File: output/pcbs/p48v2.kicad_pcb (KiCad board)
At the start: 2 copper layers, 255 x 72 mm, 147 parts, among them U1 Pico2, U2 SSD1306_OLED_1.3

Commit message: Remove Adafruit SSD1306 module (U2) from PCB
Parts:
- removed U2: SSD1306_OLED_1.3, Display:Adafruit_SSD1306_No_Mounting_Holes
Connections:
- U1 pad 26: I2C_SDA -> (no net)
- U1 pad 27: I2C_SCL -> (no net)
- U1 pad 40: VBUS -> (no net)
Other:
- net class Default removed
- net class Power removed

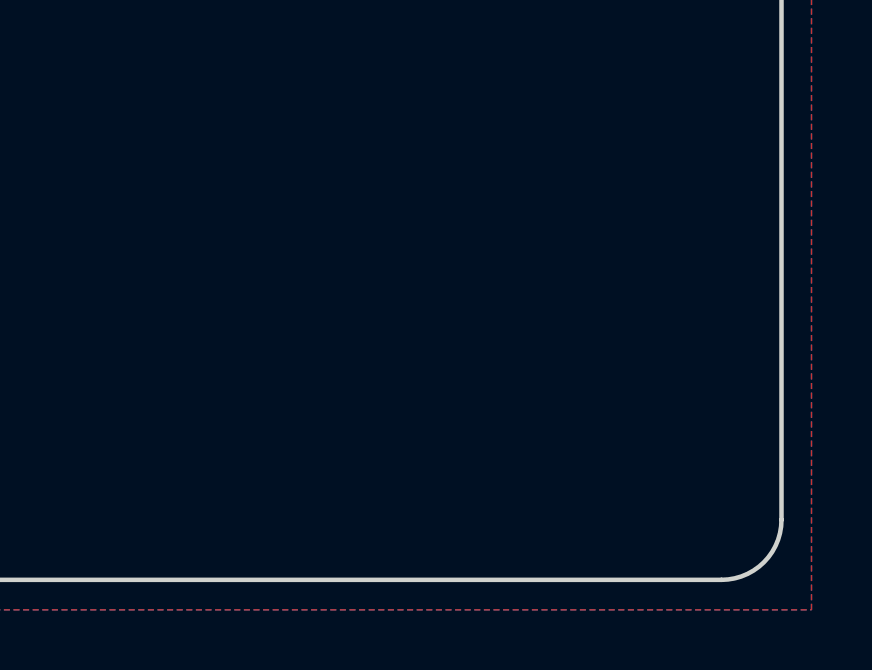
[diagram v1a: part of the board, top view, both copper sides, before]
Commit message: Place FPC connector J1 and OLED passives (C1-C6, R1-R3) on F.Cu
J1: Hirose FH12-30S-0.5SH 30-pin FPC ZIF at (333, -19)
- All 30 pins + 2 MP pads with net assignments for I2C mode
- BS0/BS1/BS2=GND (I2C), D/C=GND (addr 0x3C)
- D0=I2C_SCL, D1+D2=I2C_SDA

Passives clustered around J1:
- C1,C2: 1uF charge pump caps (C1P/C1N, C2P/C2N)
- C3: 4.7uF VCOMH bypass, C4: 2.2uF VBAT bypass
- C5,C6: 100nF VDD/VCC decoupling
- R1: 910k IREF, R2,R3: 4.7k I2C pull-ups

Placed via direct S-expression editing (MCP place_component
couldn't find footprints from standard KiCad libraries).
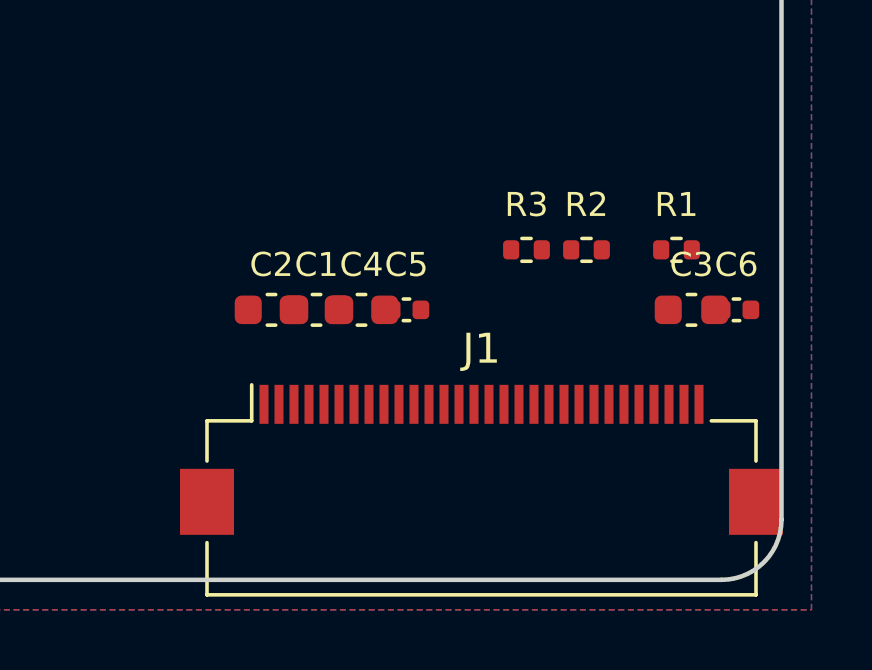
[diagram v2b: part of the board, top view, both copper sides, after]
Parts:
- added C1: 1uF, Capacitor_SMD:C_0603_1608Metric, F.Cu at (327.5, -24.0)
- added C2: 1uF, Capacitor_SMD:C_0603_1608Metric, F.Cu at (326.0, -24.0)
- added C3: 4.7uF, Capacitor_SMD:C_0603_1608Metric, F.Cu at (340.0, -24.0)
- added C4: 2.2uF, Capacitor_SMD:C_0603_1608Metric, F.Cu at (329.0, -24.0)
- added C5: 100nF, Capacitor_SMD:C_0402_1005Metric, F.Cu at (330.5, -24.0)
- added C6: 100nF, Capacitor_SMD:C_0402_1005Metric, F.Cu at (341.5, -24.0)
- added J1: FPC_30pin_0.5mm, Connector_FFC-FPC:Hirose_FH12-30S-0.5SH_1x30-1MP_P0.50mm_Horizontal, F.Cu at (333.0, -19.0)
- added R1: 910k, Resistor_SMD:R_0402_1005Metric, F.Cu at (339.5, -26.0)
- added R2: 4.7k, Resistor_SMD:R_0402_1005Metric, F.Cu at (336.5, -26.0)
- added R3: 4.7k, Resistor_SMD:R_0402_1005Metric, F.Cu at (334.5, -26.0)

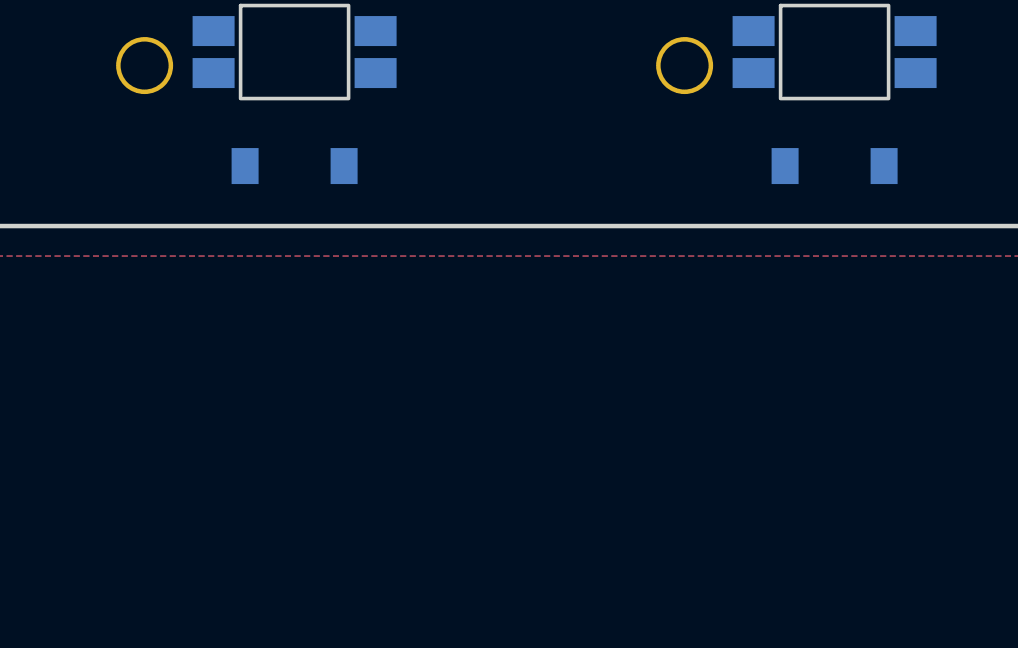
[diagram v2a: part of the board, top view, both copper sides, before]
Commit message: Add USB-C power input for LED 5V (J2, R4, R5, D49)
J2: HRO TYPE-C-31-M-12 (C165948) power-only USB-C connector
R4, R5: 5.1k CC1/CC2 pulldowns for USB-C negotiation
D49: B5819W Schottky for backfeed protection on Pico VBUS

Circuit: external 5V via J2 feeds VCC (LED rail) directly,
Pico VBUS feeds VCC through Schottky D49 to prevent backfeed.
Components at temporary position, to be moved in pcbnew.
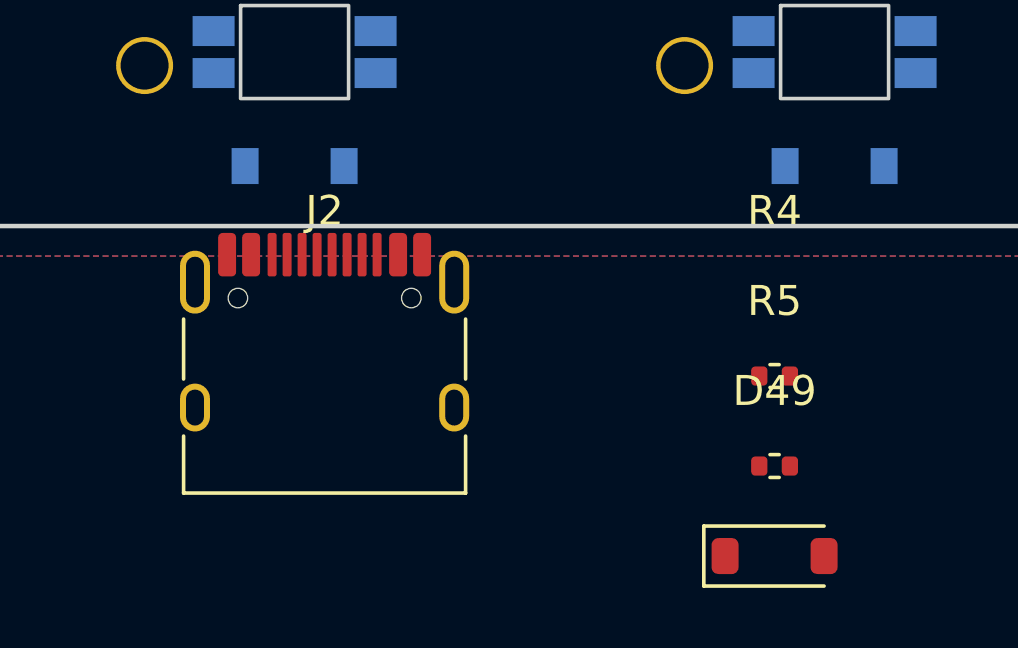
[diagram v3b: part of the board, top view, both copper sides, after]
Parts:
- added D49: B5819W, Diode_SMD:D_SOD-123, F.Cu at (295.0, -4.00)
- added J2: USB-C_Power, Connector_USB:USB_C_Receptacle_HRO_TYPE-C-31-M-12, F.Cu at (280.0, -10.0)
- added R4: 5.1k, Resistor_SMD:R_0402_1005Metric, F.Cu at (295.0, -10.0)
- added R5: 5.1k, Resistor_SMD:R_0402_1005Metric, F.Cu at (295.0, -7.00)
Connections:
- U1 pad 40: (no net) -> VBUS_PICO

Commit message: Rebuild board outline with USB-C extension and filleted corners
Extension tab (332→343, -87→-97.5) below main board for USB-C
power connector J2. All 6 corners with r=2 fillet including
concave inner corner at (332,-87) near Pico pin 1.
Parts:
- moved J2 101.0 mm to (337.5, -93.0), turned to 180 degrees
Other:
- board size 255 x 72 mm -> 255 x 82.5 mm

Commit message: Fix diode-hotswap interference, add Pico and mounting holes to ergogen
- Move diodes from B.Cu to F.Cu, shift from [0,-8.5] to [0,9.5] (above switch)
- Rewrite diode footprint with standard SOD-123 fab outline and courtyard
- Add Pico THT footprint (from AlexSutila/ergogen-footprints, KiCad 8)
- Add M2 mounting hole footprints (hole + mounting with via ring)
- Add Pico to config with full net mapping (COL0-11, ROW0-3, LED, encoder, I2C)
- Add 11 M2 mounting holes (4 corners, 3 mid-edge, 2 center, 2 extension)
- Regenerate PCB from updated ergogen config
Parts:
- removed C1, C2: 1uF, Capacitor_SMD:C_0603_1608Metric
- removed C3: 4.7uF, Capacitor_SMD:C_0603_1608Metric
- removed C4: 2.2uF, Capacitor_SMD:C_0603_1608Metric
- removed C5, C6: 100nF, Capacitor_SMD:C_0402_1005Metric
- removed D49: B5819W, Diode_SMD:D_SOD-123
- removed J1: FPC_30pin_0.5mm, Connector_FFC-FPC:Hirose_FH12-30S-0.5SH_1x30-1MP_P0.50mm_Horizontal
- removed J2: USB-C_Power, Connector_USB:USB_C_Receptacle_HRO_TYPE-C-31-M-12
- removed R1: 910k, Resistor_SMD:R_0402_1005Metric
- removed R2, R3: 4.7k, Resistor_SMD:R_0402_1005Metric
- removed R4, R5: 5.1k, Resistor_SMD:R_0402_1005Metric
- removed RE1: EC11, Rotary_Encoder:RotaryEncoder_Alps_EC11E-Switch_Vertical_H20mm
- removed U1: Pico2, Module:RaspberryPi_Pico_Common_THT
- added 19.051: , ceoloide:pico, F.Cu at (323.5, -60.5)
- added H1: , ceoloide:mountingholem2, F.Cu at (90.5, -84.5)
- added H10: , ceoloide:mountingholem2, F.Cu at (340.0, -84.5)
- added H11: , ceoloide:mountingholem2, F.Cu at (340.0, -17.5)
- added H2: , ceoloide:mountingholem2, F.Cu at (305.5, -84.5)
- added H3: , ceoloide:mountingholem2, F.Cu at (90.5, -17.5)
- added H4: , ceoloide:mountingholem2, F.Cu at (305.5, -17.5)
- added H5: , ceoloide:mountingholem2, F.Cu at (90.5, -51.0)
- added H6: , ceoloide:mountingholem2, F.Cu at (198.0, -51.0)
- added H7: , ceoloide:mountingholem2, F.Cu at (305.5, -51.0)
- added H8: , ceoloide:mountingholem2, F.Cu at (198.0, -84.5)
- added H9: , ceoloide:mountingholem2, F.Cu at (198.0, -17.5)
- D1, D10, D11, D12, D13, D14, D15, D16, D17, D18, D19, D2, D20, D21, D22, D23, D24, D25, D26, D27, D28, D29, D3, D30, D31, D32, D33, D34, D35, D36, D37, D38, D39, D4, D40, D41, D42, D43, D44, D45, D46, D47, D48, D5, D6, D7, D8, D9: moved to F.Cu
- moved D1 18.0 mm to (99.0, -35.0)
- moved D10 18.0 mm to (135.0, -52.0)
- moved D11 18.0 mm to (135.0, -69.0)
- moved D12 18.0 mm to (135.0, -86.0)
- moved D13 18.0 mm to (153.0, -35.0)
- moved D14 18.0 mm to (153.0, -52.0)
- moved D15 18.0 mm to (153.0, -69.0)
- moved D16 18.0 mm to (153.0, -86.0)
- moved D17 18.0 mm to (171.0, -35.0)
- moved D18 18.0 mm to (171.0, -52.0)
- moved D19 18.0 mm to (171.0, -69.0)
- moved D2 18.0 mm to (99.0, -52.0)
- moved D20 18.0 mm to (171.0, -86.0)
- moved D21 18.0 mm to (189.0, -35.0)
- moved D22 18.0 mm to (189.0, -52.0)
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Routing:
- removed copper zone on B.Cu, net GND
- removed copper zone on F.Cu, net GND
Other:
- board size 255 x 82.5 mm -> 255 x 72 mm

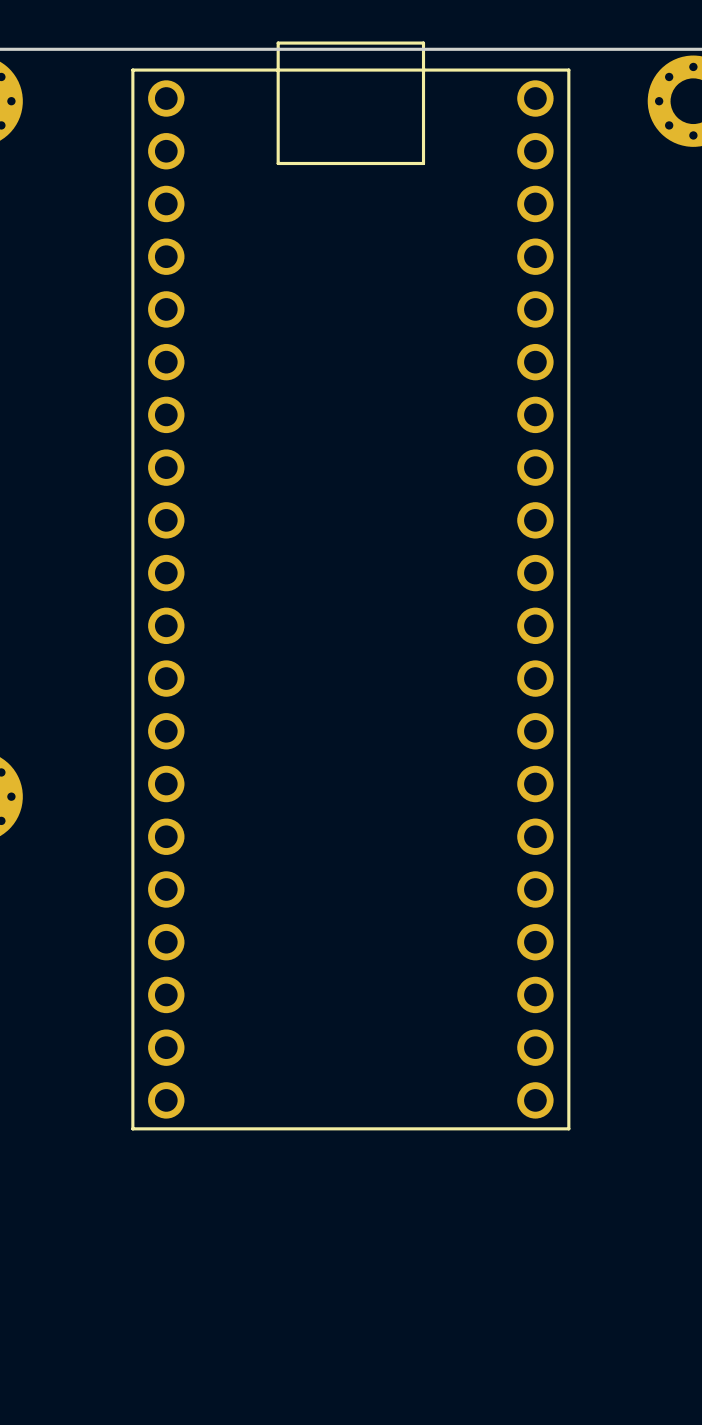
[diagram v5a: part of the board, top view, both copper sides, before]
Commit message: Add USB-C power footprint, 0603 resistor, and Pico castellated option
New ergogen footprints:
- usb_c_hro_type_c_31_m_12.js: HRO TYPE-C-31-M-12 USB-C receptacle
- resistor_0603.js: 0603 HandSolder SMD resistor

Pico footprint now supports castellated mounting (SMD pads at board edge)
via castellated: true param. Config updated to use castellated on B.Cu.

Config additions: J2 (USB-C power), R4/R5 (CC pulldowns), D49 (Schottky)
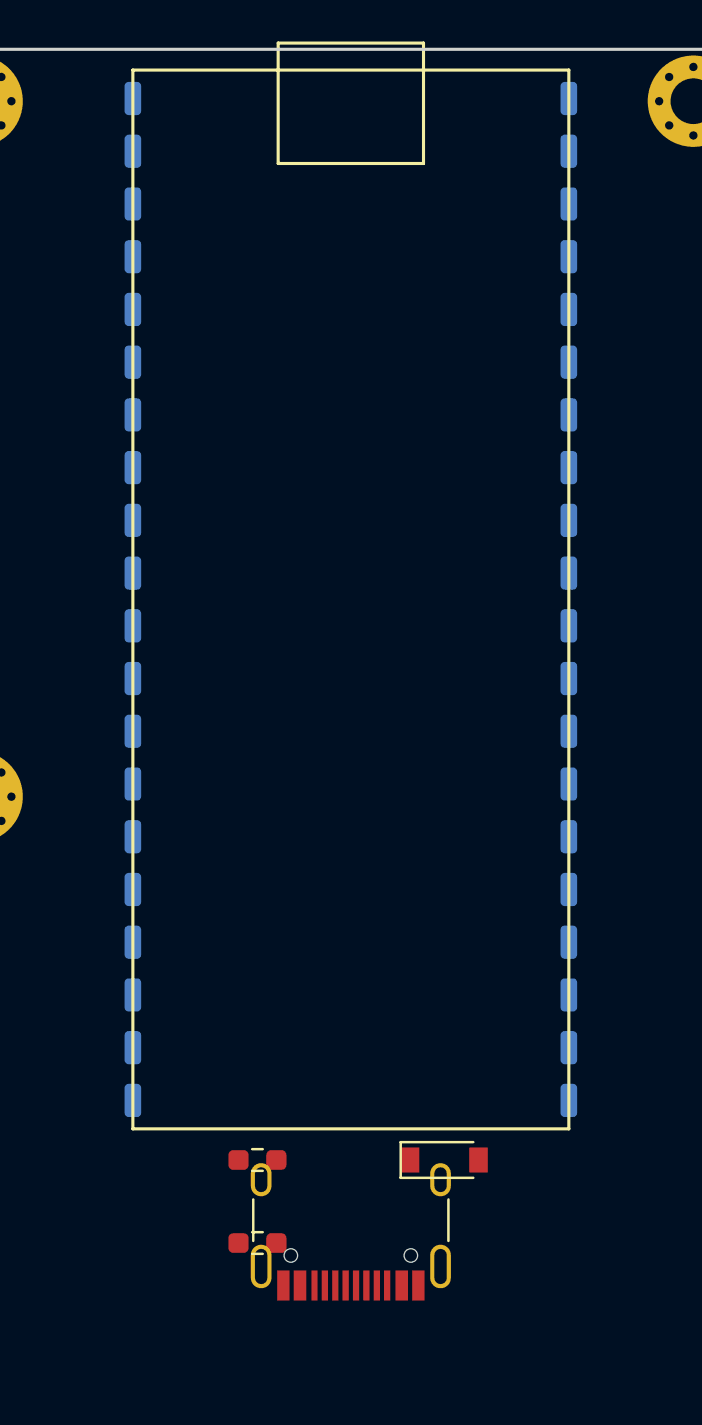
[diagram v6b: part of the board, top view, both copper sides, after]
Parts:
- added D49: , ceoloide:diode_tht_sod123, F.Cu at (328.0, -33.5)
- added J1: , ceoloide:usb_c_hro_type_c_31_m_12, F.Cu at (323.5, -31.5)
- added R1: , ceoloide:resistor_0603, F.Cu at (319.0, -33.5)
- added R2: , ceoloide:resistor_0603, F.Cu at (319.0, -29.5)

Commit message: Enlarge Pico castellated pads, add Power netclass 1.0mm track
Pico castellated pads: 4.8x1.6mm at board edge with 50% more exposed area.
Power netclass: 1.0mm track, 0.3mm clearance, 0.8/0.4mm via.
Assigned VCC, VBUS, GND, VSYS, OUT_3V3, VCC_3V3 to Power class.
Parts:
- moved R2 48.9 mm to (330.5, -77.0), turned to 180 degrees
- moved J1 46.7 mm to (339.0, -75.5), turned to 90 degrees
- moved R1 42.6 mm to (330.5, -74.5), turned to 180 degrees
- moved D49 38.5 mm to (328.0, -72.0), turned to 180 degrees
- moved 19.051 1.00 mm to (322.5, -60.5)
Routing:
- net USB2_CC2: track 0.00 -> 3.65 mm
- net USB2_CC1: track 0.00 -> 3.65 mm

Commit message: Manual KiCad edits: routing and board setup
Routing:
- net VCC: track 0.00 -> 1267.6 mm, vias 0 -> 35
- net COL1: track 0.00 -> 342.5 mm, vias 0 -> 8
- net COL0: track 0.00 -> 323.4 mm, vias 0 -> 4
- net COL2: track 0.00 -> 286.7 mm, vias 0 -> 2
- net COL5: track 0.00 -> 284.5 mm, vias 0 -> 2
- net COL4: track 0.00 -> 272.6 mm, vias 0 -> 2
- net COL3: track 0.00 -> 270.9 mm, vias 0 -> 2
- net COL6: track 0.00 -> 254.9 mm
- net COL7: track 0.00 -> 235.2 mm, vias 0 -> 4
- net ROW0: track 0.00 -> 214.6 mm
- net COL8: track 0.00 -> 210.1 mm, vias 0 -> 4
- net ROW2: track 0.00 -> 208.2 mm
- net ROW1: track 0.00 -> 206.2 mm
- net ROW3: track 0.00 -> 188.4 mm
- net COL10: track 0.00 -> 162.7 mm, vias 0 -> 6
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- added copper zone on B.Cu, net GND
- added copper zone on F.Cu, net GND
